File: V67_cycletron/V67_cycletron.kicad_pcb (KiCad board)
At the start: 2 copper layers, 102.1 x 110.1 mm, 54 parts, among them J1 USB_C_Receptacle_USB2.0_16P, J3 Screw_Terminal_01x11, U1 LM1117DT-5.0, U2 LM1117DT-3.3, U3 ESP32-S3-WROOM-1

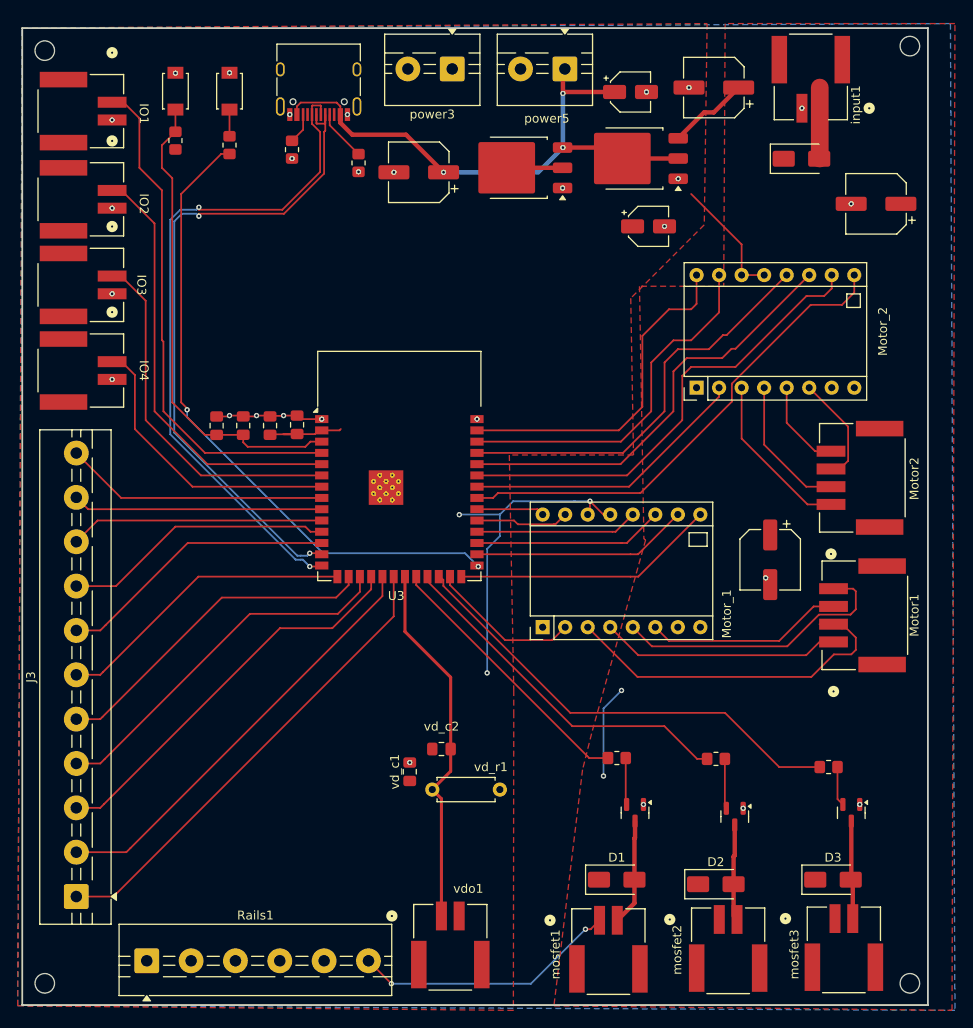
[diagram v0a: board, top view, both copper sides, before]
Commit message: fixed drc, added silscreen notes, made certain vias bigger
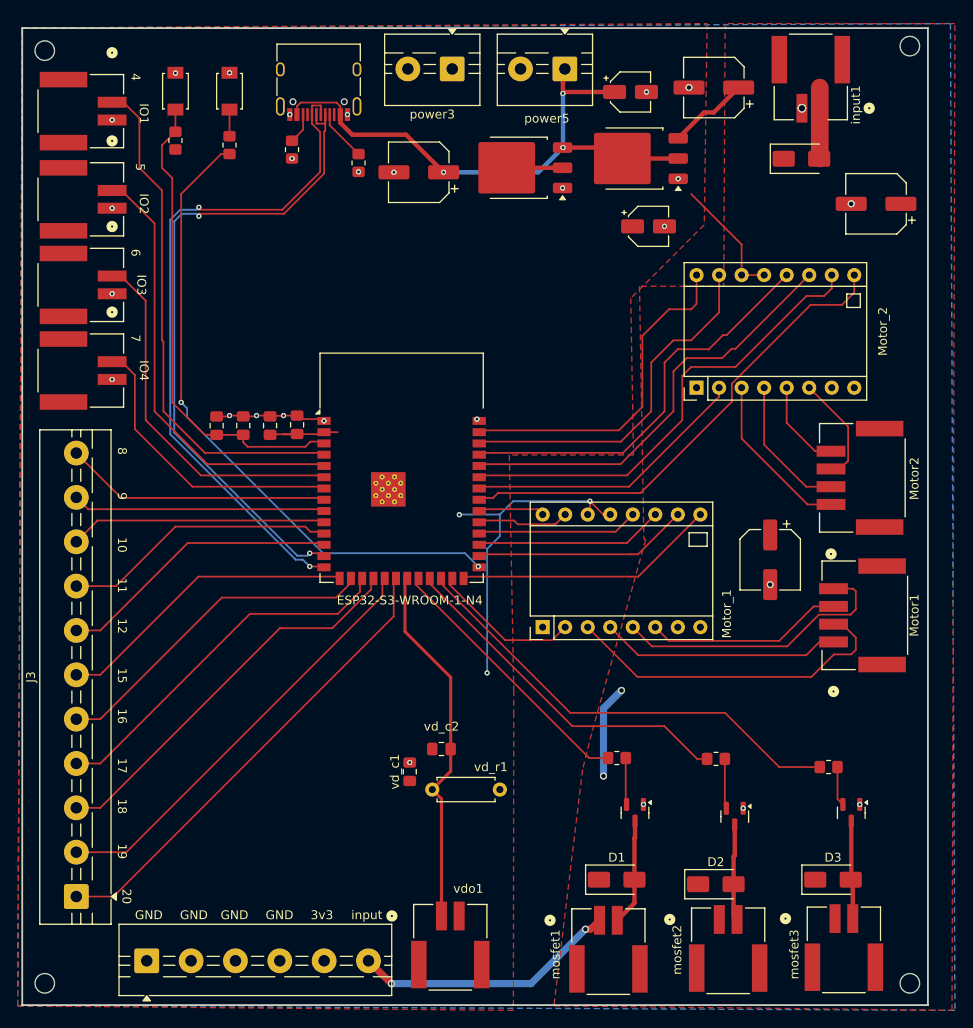
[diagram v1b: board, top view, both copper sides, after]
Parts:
- removed U3: ESP32-S3-WROOM-1, RF_Module:ESP32-S3-WROOM-1
- added ESP32-S3-WROOM-1-N4: ESP32-S3-WROOM-1, RF_Module:ESP32-S3-WROOM-1, F.Cu at (143.4, 68.3)
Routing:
- net 3V3: track 69.9 -> 69.4 mm
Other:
- board text added: "10"
- board text added: "11"
- board text added: "12"
- board text added: "15"
- board text added: "16"
- board text added: "17"
- board text added: "18"
- board text added: "19"
- board text added: "20"
- board text added: "3v3"
- board text added: "4"
- board text added: "5"
- board text added: "6"
- board text added: "7"
- board text added: "8"
- board text added: "9"
- board text added: "GND"
- board text added: "input"

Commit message: purchased boards
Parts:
- added D4: LED, LED_SMD:LED_0603_1608Metric_Pad1.05x0.95mm_HandSolder, F.Cu at (177.7, 38.1)
- added D5: LED, LED_SMD:LED_0603_1608Metric_Pad1.05x0.95mm_HandSolder, F.Cu at (182.7, 38.1)
- added R3: 1k, Resistor_SMD:R_0805_2012Metric_Pad1.20x1.40mm_HandSolder, F.Cu at (179.8, 35.6)
- added R4: 4.7k, Resistor_SMD:R_0805_2012Metric_Pad1.20x1.40mm_HandSolder, F.Cu at (182.9, 40.6)
- moved Motor1 5.45 mm to (196.1, 90.4)
- moved J3 4.12 mm to (106.7, 120.8)
- moved IO4 3.56 mm to (107.2, 61.0)
- moved IO3 2.54 mm to (107.2, 50.3)
- moved IO2 1.02 mm to (107.2, 39.1)
- moved IO1 0.22 mm to (107.2, 27.9)
- moved U4 0.09 mm to (143.4, 68.3)
- renumbered ESP32-S3-WROOM-1-N4 to U4
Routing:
- net Motor1_B2: track 20.8 -> 31.6 mm
- net Motor1_A2: track 41.1 -> 30.8 mm
- net Motor1_A1: track 25.5 -> 34.1 mm
- net Motor1_B1: track 32.4 -> 25.2 mm
- net IO7: track 33.0 -> 29.5 mm
- net Net-(D4-K): track 0.00 -> 2.66 mm
- net IO6: track 41.7 -> 39.0 mm
- net Net-(D5-K): track 0.00 -> 2.64 mm
- net I16: track 37.9 -> 39.8 mm
- net I15: track 34.0 -> 35.9 mm
- net I12: track 31.8 -> 33.5 mm
- net I11: track 30.7 -> 32.4 mm
- net I10: track 28.7 -> 30.4 mm
- net I08: track 29.8 -> 28.1 mm
- net I20: track 53.3 -> 54.9 mm
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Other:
- board text added: "+"
- board text added: "-"
- board text added: "Dev: Ryan Taylor"
- board text added: "ESP32-S3-WROOM-1-N16"
